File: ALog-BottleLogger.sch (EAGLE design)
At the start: 103 parts, among them IC2 ATMEGA644M, Q1 220mA/50V/3.5Ω, Q11 220mA/50V/3.5Ω, Q12 4.3A/20V/54mΩ, Q5 4.3A/20V/54mΩ, Q6 4.3A/20V/54mΩ, Q7 4.3A/20V/54mΩ, Q8 220mA/50V/3.5Ω, Q9 220mA/50V/3.5Ω, U2 FT231X-Q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

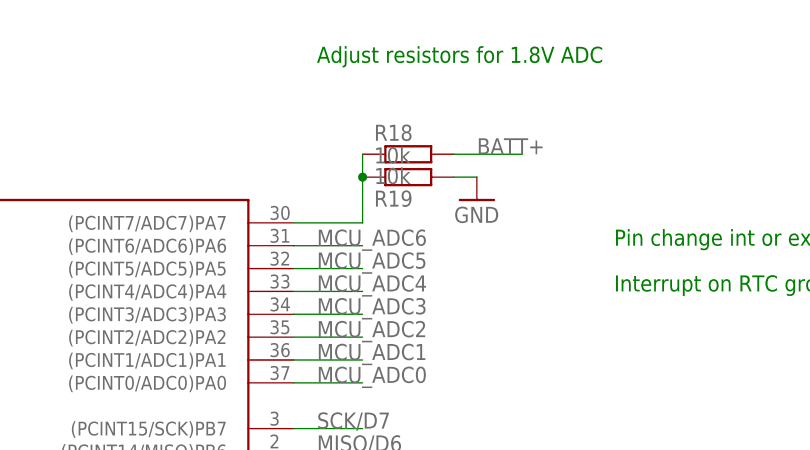
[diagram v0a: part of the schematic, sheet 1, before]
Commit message: COM on ADC should be 2.5V divided from 5V not GND
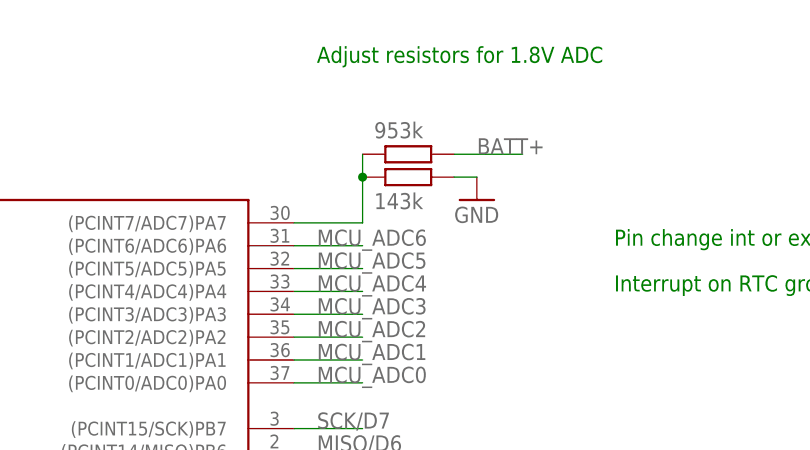
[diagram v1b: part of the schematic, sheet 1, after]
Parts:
- R18: value 10k -> 953k
- R19: value 10k -> 143k
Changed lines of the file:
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@@
 <part name="GND52" library="supply1" deviceset="GND" device=""/>
 <part name="S1" library="Custom" deviceset="SKRPABE010" device=""/>
-<part name="R18" library="rcl" deviceset="R-EU_" device="R0603" value="10k"/>
-<part name="R19" library="rcl" deviceset="R-EU_" device="R0603" value="10k"/>
+<part name="R18" library="rcl" deviceset="R-EU_" device="R0603" value="953k"/>
+<part name="R19" library="rcl" deviceset="R-EU_" device="R0603" value="143k"/>
 <part name="GND54" library="supply1" deviceset="GND" device=""/>
 <part name="+3V1" library="supply1" deviceset="+3V3" device=""/>
@@
 <attribute name="NAME" x="274.32" y="1.524" size="1.778" layer="95" font="vector" align="bottom-center"/>
 </instance>
-<instance part="R18" gate="G$1" x="254" y="60.96"/>
-<instance part="R19" gate="G$1" x="254" y="58.42" rot="MR180"/>
+<instance part="R18" gate="G$1" x="254" y="60.96" smashed="yes">
+<attribute name="VALUE" x="250.19" y="62.738" size="1.778" layer="96"/>
+</instance>
+<instance part="R19" gate="G$1" x="254" y="58.42" smashed="yes" rot="MR180">
+<attribute name="VALUE" x="250.19" y="56.642" size="1.778" layer="96" rot="MR180"/>
+</instance>
 <instance part="GND54" gate="1" x="261.62" y="55.88"/>
 <instance part="+3V1" gate="G$1" x="439.42" y="40.64"/>

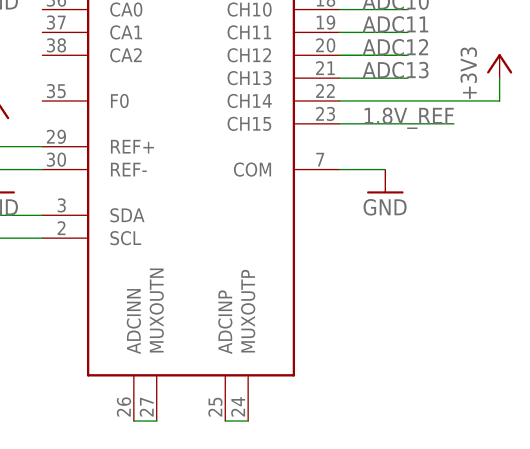
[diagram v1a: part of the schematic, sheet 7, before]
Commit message: improved 3V3 component layout
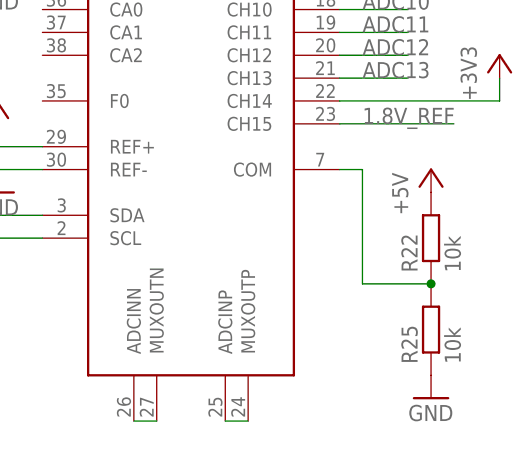
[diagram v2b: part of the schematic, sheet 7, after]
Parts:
- added C4: 10uF, rcl:C-EUC0805
- added R22, R25: 10k, rcl:R-EU_R0603
- R15, R19: value 143k -> 111k
- R16, R18: value 953k -> 1M
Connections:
- new net N$16: R22.1, R25.2, U$7.COM
- net +5V: now also C4.1, R22.2
- net GND: now also C4.2, R25.1; no longer U$7.COM
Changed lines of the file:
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@@
 <?xml version="1.0" encoding="utf-8"?>
 <!DOCTYPE eagle SYSTEM "eagle.dtd">
-<eagle version="8.2.2">
+<eagle version="8.4.0">
 <drawing>
 <settings>
 <setting alwaysvectorfont="no"/>
+<setting keepoldvectorfont="yes"/>
 <setting verticaltext="up"/>
 </settings>
@@
 <part name="GND40" library="SparkFun-PowerSymbols" deviceset="GND" device=""/>
 <part name="C25" library="rcl" deviceset="C-EU" device="C0805" value="10uF"/>
-<part name="R15" library="rcl" deviceset="R-EU_" device="R0603" value="143k"/>
-<part name="R16" library="rcl" deviceset="R-EU_" device="R0603" value="953k"/>
+<part name="R15" library="rcl" deviceset="R-EU_" device="R0603" value="111k"/>
+<part name="R16" library="rcl" deviceset="R-EU_" device="R0603" value="1M"/>
 <part name="C1" library="rcl" deviceset="C-EU" device="C0805" value="22uF"/>
 <part name="C2" library="rcl" deviceset="C-EU" device="C0805" value="22uF"/>
@@
 <part name="GND52" library="supply1" deviceset="GND" device=""/>
 <part name="S1" library="Custom" deviceset="SKRPABE010" device=""/>
-<part name="R18" library="rcl" deviceset="R-EU_" device="R0603" value="953k"/>
-<part name="R19" library="rcl" deviceset="R-EU_" device="R0603" value="143k"/>
+<part name="R18" library="rcl" deviceset="R-EU_" device="R0603" value="1M"/>
+<part name="R19" library="rcl" deviceset="R-EU_" device="R0603" value="111k"/>
 <part name="GND54" library="supply1" deviceset="GND" device=""/>
 <part name="+3V1" library="supply1" deviceset="+3V3" device=""/>
@@
 <part name="C6" library="rcl" deviceset="C-EU" device="C0603" value="0.1uF"/>
 <part name="GND7" library="supply1" deviceset="GND" device=""/>
-<part name="GND8" library="supply1" deviceset="GND" device=""/>
 <part name="GND9" library="supply1" deviceset="GND" device=""/>
 <part name="GND10" library="supply1" deviceset="GND" device=""/>
@@
 <part name="R20" library="rcl" deviceset="R-EU_" device="R0603" value="10k"/>
 <part name="U$6" library="csandell" deviceset="74404020022" device=""/>
+<part name="R22" library="rcl" deviceset="R-EU_" device="R0603" value="10k"/>
+<part name="R25" library="rcl" deviceset="R-EU_" device="R0603" value="10k"/>
+<part name="P+1" library="supply1" deviceset="+5V" device=""/>
+<part name="GND8" library="supply1" deviceset="GND" device=""/>
+<part name="GND18" library="supply1" deviceset="GND" device=""/>
+<part name="C4" library="rcl" deviceset="C-EU" device="C0805" value="10uF"/>
 </parts>
 <sheets>
@@
 <instance part="+3V4" gate="G$1" x="-20.32" y="66.04"/>
 <instance part="P+2" gate="1" x="0" y="111.76"/>
-<instance part="P+3" gate="1" x="-83.82" y="58.42"/>
+<instance part="P+3" gate="1" x="-88.9" y="63.5"/>
 <instance part="U$2" gate="G$1" x="-60.96" y="10.16"/>
 <instance part="+3V15" gate="G$1" x="-73.66" y="20.32"/>
@@
 <attribute name="VALUE" x="-30.48" y="59.69" size="1.778" layer="96" rot="R180"/>
 </instance>
+<instance part="GND18" gate="1" x="-91.44" y="40.64"/>
+<instance part="C4" gate="G$1" x="-91.44" y="48.26"/>
 </instances>
 <busses>
@@
 <pinref part="GND5" gate="1" pin="GND"/>
 <wire x1="-40.64" y1="5.08" x2="-40.64" y2="2.54" width="0.1524" layer="91"/>
+</segment>
+<segment>
+<pinref part="C4" gate="G$1" pin="2"/>
+<pinref part="GND18" gate="1" pin="GND"/>
 </segment>
 </net>
@@
 <pinref part="U$3" gate="G$1" pin="VIN"/>
 <wire x1="-81.28" y1="55.88" x2="-76.2" y2="55.88" width="0.1524" layer="91"/>
-<wire x1="-83.82" y1="55.88" x2="-81.28" y2="55.88" width="0.1524" layer="91"/>
 <pinref part="P+3" gate="1" pin="+5V"/>
+<wire x1="-81.28" y1="55.88" x2="-88.9" y2="55.88" width="0.1524" layer="91"/>
+<wire x1="-88.9" y1="55.88" x2="-88.9" y2="60.96" width="0.1524" layer="91"/>
+<junction x="-81.28" y="55.88"/>
+<pinref part="C4" gate="G$1" pin="1"/>
+<wire x1="-81.28" y1="53.34" x2="-91.44" y2="53.34" width="0.1524" layer="91"/>
+<wire x1="-91.44" y1="53.34" x2="-91.44" y2="50.8" width="0.1524" layer="91"/>
+<junction x="-81.28" y="53.34"/>
 </segment>
 </net>
@@
 <instance part="P+8" gate="1" x="38.1" y="40.64"/>
 <instance part="+3V6" gate="G$1" x="109.22" y="55.88"/>
-<instance part="GND8" gate="1" x="96.52" y="40.64"/>
 <instance part="GND9" gate="1" x="53.34" y="63.5"/>
 <instance part="GND10" gate="1" x="53.34" y="40.64"/>
 <instance part="P+6" gate="1" x="53.34" y="50.8"/>
+<instance part="R22" gate="G$1" x="101.6" y="35.56" rot="R90"/>
+<instance part="R25" gate="G$1" x="101.6" y="25.4" rot="R90"/>
+<instance part="P+1" gate="1" x="101.6" y="43.18"/>
+<instance part="GND8" gate="1" x="101.6" y="17.78"/>
 </instances>
 <busses>
@@
 </segment>
 <segment>
-<pinref part="U$7" gate="G$1" pin="COM"/>
-<wire x1="91.44" y1="43.18" x2="96.52" y2="43.18" width="0.1524" layer="91"/>
-<pinref part="GND8" gate="1" pin="GND"/>
-</segment>
-<segment>
 <pinref part="U$7" gate="G$1" pin="REF-"/>
 <wire x1="58.42" y1="43.18" x2="53.34" y2="43.18" width="0.1524" layer="91"/>
 <pinref part="GND10" gate="1" pin="GND"/>
+</segment>
+<segment>
+<pinref part="R25" gate="G$1" pin="1"/>
+<pinref part="GND8" gate="1" pin="GND"/>
 </segment>
 </net>
@@
 <pinref part="P+6" gate="1" pin="+5V"/>
 </segment>
+<segment>
+<pinref part="R22" gate="G$1" pin="2"/>
+<pinref part="P+1" gate="1" pin="+5V"/>
+</segment>
 </net>
 <net name="1.8V_REF" class="0">
@@
 </segment>
 </net>
+<net name="N$16" class="0">
+<segment>
+<pinref part="R22" gate="G$1" pin="1"/>
+<pinref part="R25" gate="G$1" pin="2"/>
+<pinref part="U$7" gate="G$1" pin="COM"/>
+<wire x1="91.44" y1="43.18" x2="93.98" y2="43.18" width="0.1524" layer="91"/>
+<wire x1="93.98" y1="43.18" x2="93.98" y2="30.48" width="0.1524" layer="91"/>
+<wire x1="93.98" y1="30.48" x2="101.6" y2="30.48" width="0.1524" layer="91"/>
+<junction x="101.6" y="30.48"/>
+</segment>
+</net>

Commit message: Final revisions made, many changes, 5V external mosphet update, RTC power configuration, add 5V psync control pin, change external power control pins, add barrel jack, rerouted whole board
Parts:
- removed F3, F4: 6V/0.5A, SparkFun-Fuses:PPTC_HALF-AMP
- removed L_LPF: 10uH, SparkFun:INDUCTOR0805
- removed Q1: 220mA/50V/3.5Ω, SparkFun-DiscreteSemi:MOSFET-NCH-BSS138
- removed Q6: 4.3A/20V/54mΩ, SparkFun-DiscreteSemi:MOSFET_PCH-IRLML2244
- removed R21, R7: 10k, rcl:R-EU_R0603
- removed RCKL2, RCLK1: 220, rcl:R-US_R0603
- added C7: 0.1uF, rcl:C-EUC0603
- added F1, F2: PPTC_HALF-AMP, bschulz:PPTC_HALF-AMP
- added J6: 5.5x2.1mm Barrel, bschulz:POWER_JACKSMD
- added Q10: MOSFET_PCH-IRLML2244, bschulz:MOSFET_PCH-IRLML2244
- added Q13: MOSFET-NCH-BSS138, bschulz:MOSFET-NCH-BSS138
- added R26: 10k, bschulz:R-EU_10KR0603
- added R27: (no value), bschulz:R-EU_10KR0603
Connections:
- removed net AVCC: ADECOUP.1, IC2.AVCC, L_LPF.2
- removed net MCU_ADC2: IC2.(PCINT2/ADC2)PA2
- removed net MCU_ADC3: IC2.(PCINT3/ADC3)PA3
- removed net N$14: F4.2, Q6.S
- removed net N$31: D2.A2, RCKL2.1
- removed net N$38: D2.A1, RCLK1.1
- removed net RTC_BATT: CLOCK_BATT.+, RCLK1.2
- removed net RTC_EN: IC2.(PCINT9/CLKO/T1)PB1, RTC1.VCC
- new net D20: IC2.(PCINT20/TDO)PC4
- new net D22: IC2.(PCINT22/TOSC1)PC6
- new net N$20: F2.1, Q10.D
- new net N$23: Q10.G, Q13.D, R26.2
- new net PSYNC: IC2.(PCINT9/CLKO/T1)PB1, U3.PSYNC
- net +3V3: now also ADECOUP.1, D2.A2, IC2.AREF, IC2.AVCC, R27.2; no longer L_LPF.1, R21.2, RCKL2.2
- net +5V: now also Q10.S, R26.1; no longer Q6.D, R7.2
- net 1.8V_REF: no longer IC2.AREF
- net 3.3V_EXT_CTRL: now also IC2.(PCINT2/ADC2)PA2; no longer IC2.(PCINT22/TOSC1)PC6
- net 5V_EXT_CTRL: now also IC2.(PCINT3/ADC3)PA3, Q13.G, R27.1; no longer IC2.(PCINT20/TDO)PC4, Q1.G, R21.1
- net BATT+: now also J6.PWR
- net EXT_3.3V: now also F1.2; no longer F3.2
- net EXT_5V: now also F2.2; no longer F4.1
- net GND: now also C7.2, J6.GND, J6.GNDBREAK, Q13.S, RTC1.VCC; no longer Q1.S
- net N$17: now also F1.1; no longer F3.1
- net N$37: now also C7.1
- net N$6: now also CLOCK_BATT.+, D2.A1; no longer Q1.D, Q6.G, R7.1
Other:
- note added: "Power In (From battery)"

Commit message: Updated part data
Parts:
- ADECOUP, C40: device resistor:C-EUC0603 -> bschulz_passives:C-EU0.1UFC0603
- C1, C10, C2, C24: device rcl:C-EUC0805 -> bschulz_passives:C-EU22UFC0805
- C13, C15, C16, C17, C18, C28, C29, C3, C30, C31, C32, C33, C34, C35, C43, C7: device rcl:C-EUC0603 -> bschulz_passives:C-EU0.1UFC0603
- C22, C25, C4: device rcl:C-EUC0805 -> bschulz_passives:C-EU10UFC0805
- D+, D-: device rcl:R-US_R0603 -> bschulz_passives:R-EU_27R0603
- IC2: device atmel:ATMEGA644M -> bschulz:ATMEGA644M
- J1, J14, J15, J16, J2, J8: device SparkFun-Connectors:CONN_10 -> bschulz:CONN_103.5MM
- J4: device SparkFun-Connectors:JST_2MM_MALE -> bschulz:JST_2MM_MALE
- MICRO_USB: value 10118194-0001LF_LONGER_PADS -> MICRO_USB_LONGPADS; device 10118194-0001LF:10118194-0001LF_LONGER_PADS -> bschulz:MICRO_USB_LONGPADS
- Q11, Q8, Q9: value 220mA/50V/3.5Ω -> MOSFET-NCH-BSS138; device SparkFun-DiscreteSemi:MOSFET-NCH-BSS138 -> bschulz:MOSFET-NCH-BSS138
- Q12, Q5, Q7: value 4.3A/20V/54mΩ -> MOSFET_PCH-IRLML2244; device SparkFun-DiscreteSemi:MOSFET_PCH-IRLML2244 -> bschulz:MOSFET_PCH-IRLML2244
- R1, R11, R12, R17, R2, R22, R23, R24, R25, R3, R43, R6, R8, R9: device rcl:R-EU_R0603 -> bschulz_passives:R-EU_10KR0603
- R16: device rcl:R-EU_R0603 -> bschulz_passives:R-EU_R0603
- R26: device bschulz:R-EU_10KR0603 -> bschulz_passives:R-EU_10KR0603
- R27: value (none) -> 10k
- RTC1: device SparkFun-Clocks:DS3231M -> bschulz:DS3231M
- R_LED1: device resistor:R-US_R0603 -> bschulz_passives:R-EU_R0603
- S1, U$4: device Custom:SKRPABE010 -> bschulz:SKRPABE010
- U$2: value MAX6070 -> MAX6070AAUT18; device bschulz:MAX6070 -> bschulz:MAX6070AAUT18
- U$3: value TPS62172 -> TPS62172-Q1; device SparkFun-IC-Power:TPS62172 -> bschulz:TPS62172-Q1
- U$7: device linear-technology:LTC2495 -> bschulz:LTC2495
- U2: device FT231X:FT231X-Q -> bschulz:FT231X-Q
- U3: device microbuilder:VREG_TPS63060/1 -> bschulz:TPS63060

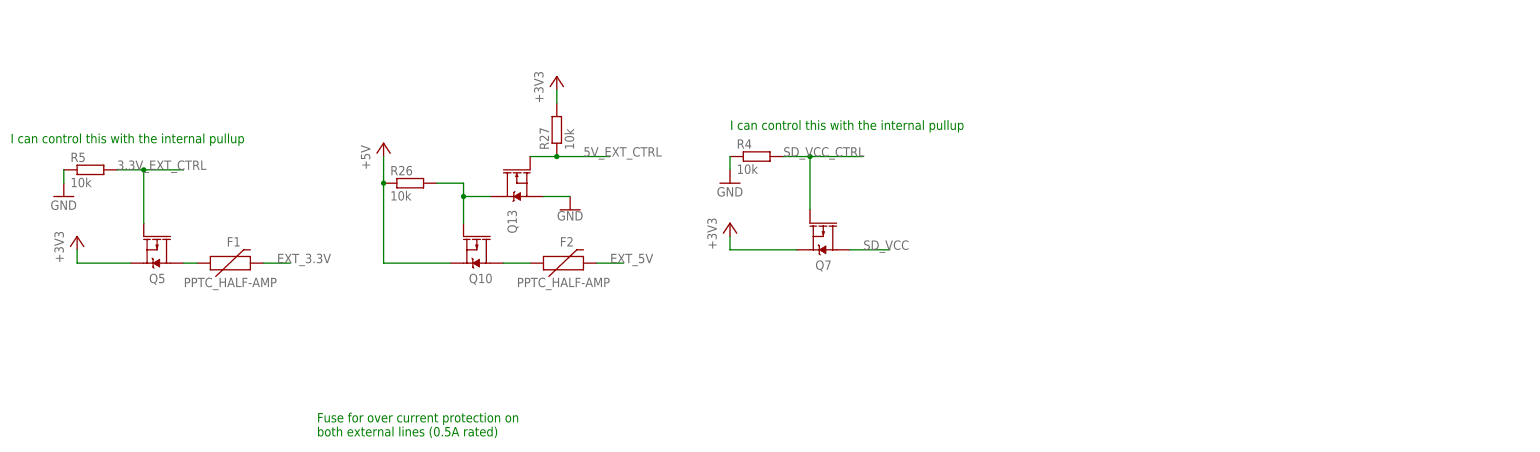
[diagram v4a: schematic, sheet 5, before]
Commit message: Added comparators, added SCL/SDA connections, updated resistor values and voltage divider sources
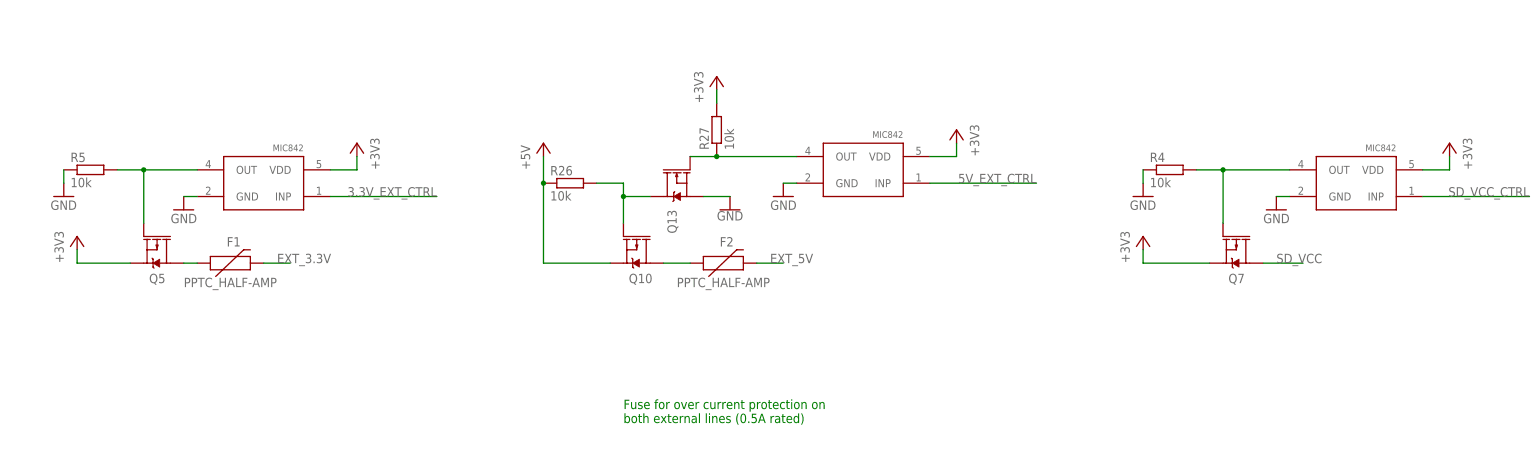
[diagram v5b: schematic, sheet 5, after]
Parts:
- removed D2: BAT54C, semicon-smd-ipc:DIODE_AC-CA_
- added U$1, U$12, U$16: MIC842, Custom:MIC842
- R15, R19: value 111k -> 180k; device rcl:R-EU_R0603 -> bschulz_passives:R-EU_180KR0603
- R16: value 1M -> 1.62M; device bschulz_passives:R-EU_R0603 -> bschulz_passives:R-EU_1.62MR0603
- R18: value 1M -> 1.62M; device rcl:R-EU_R0603 -> bschulz_passives:R-EU_1.62MR0603
- R22: value 10k -> 180k; device bschulz_passives:R-EU_10KR0603 -> bschulz_passives:R-EU_180KR0603
- R25: value 10k -> 180k; device bschulz_passives:R-EU_10KR0603 -> bschulz_passives:R-EU_180KR0603; DIGIKEY (none) -> 311-180KLDCT-ND; MPN (none) -> AC0603FR-07180KL; VALUE_PART (none) -> 180k
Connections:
- new net N$14: Q13.G, R27.1, U$1.OUT
- new net N$19: Q7.G, R4.2, U$16.OUT
- net +3V3: now also U$1.VDD, U$12.VDD, U$16.VDD; no longer D2.A2
- net 3.3V_EXT_CTRL: now also U$12.INP; no longer Q5.G, R5.2
- net 5V_EXT_CTRL: now also U$1.INP; no longer Q13.G, R27.1
- net EXT_3.3V: now also RTC1.VCC; no longer J14.2, J15.2, J16.2
- net GND: now also U$1.GND, U$12.GND, U$16.GND; no longer J14.1, J15.1, J16.1, RTC1.VCC
- net N$37: now also CLOCK_BATT.+; no longer D2.K
- net N$6: now also Q5.G, R5.2, U$12.OUT; no longer CLOCK_BATT.+, D2.A1
- net SCL: now also J14.1, J15.1, J16.1
- net SDA: now also J14.2, J15.2, J16.2
- net SD_VCC_CTRL: now also U$16.INP; no longer Q7.G, R4.2
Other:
- note removed: "Control line for REF_EN"
- note removed: "I can control this with the internal pullup"
- moved on the sheet: F2, Q10, Q13, Q7, R26, R27, R4

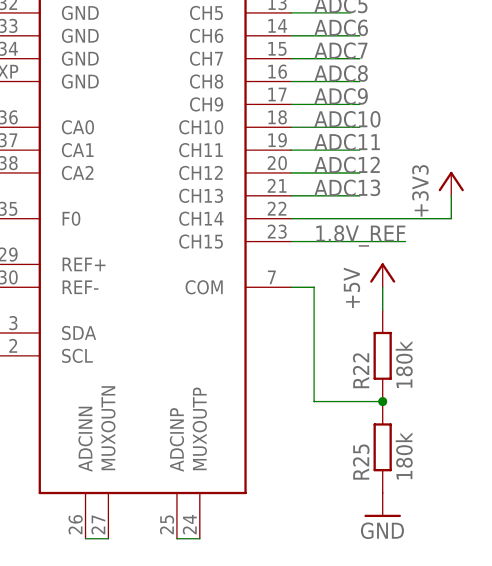
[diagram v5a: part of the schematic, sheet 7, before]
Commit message: EXT_5V on COM voltage divider on ADC
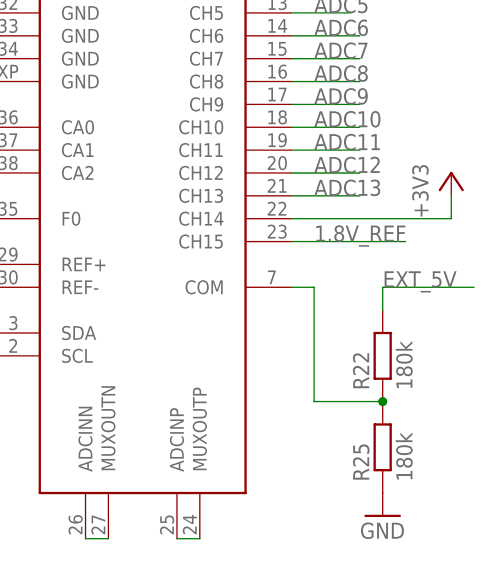
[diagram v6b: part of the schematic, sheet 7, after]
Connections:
- net +5V: no longer R22.2
- net EXT_5V: now also R22.2
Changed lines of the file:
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@@
 <attribute name="VALUE_PART" value="180k"/>
 </part>
-<part name="P+1" library="supply1" deviceset="+5V" device=""/>
 <part name="GND8" library="supply1" deviceset="GND" device=""/>
 <part name="GND18" library="supply1" deviceset="GND" device=""/>
@@
 <instance part="R22" gate="G$1" x="101.6" y="35.56" rot="R90"/>
 <instance part="R25" gate="G$1" x="101.6" y="25.4" rot="R90"/>
-<instance part="P+1" gate="1" x="101.6" y="45.72"/>
 <instance part="GND8" gate="1" x="101.6" y="17.78"/>
 </instances>
@@
 <pinref part="P+6" gate="1" pin="+5V"/>
 </segment>
-<segment>
-<pinref part="R22" gate="G$1" pin="2"/>
-<pinref part="P+1" gate="1" pin="+5V"/>
-<wire x1="101.6" y1="43.18" x2="101.6" y2="40.64" width="0.1524" layer="91"/>
-</segment>
 </net>
 <net name="1.8V_REF" class="0">
@@
 </segment>
 </net>
+<net name="EXT_5V" class="0">
+<segment>
+<pinref part="R22" gate="G$1" pin="2"/>
+<wire x1="101.6" y1="40.64" x2="101.6" y2="43.18" width="0.1524" layer="91"/>
+<wire x1="101.6" y1="43.18" x2="111.76" y2="43.18" width="0.1524" layer="91"/>
+<label x="101.6" y="43.18" size="1.778" layer="95"/>
+</segment>
+</net>
